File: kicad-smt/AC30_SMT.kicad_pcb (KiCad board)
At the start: 2 copper layers, 173 x 88.5 mm, 122 parts, among them IC1 4013, IC10 555, IC11 4001, IC12 1489, IC13 4070, IC14 4053, IC15 1488, IC2 4001, IC3 4070, IC4 4558, IC5 4013, IC6 4053, IC7 4049, IC8 4013, IC9 4023, J1 SWITCHES, J12 Power input, J13 MOTOR, J14 MIC, J15 EAR, J2 LEDS, J3 Computer interface (COMP), J4 Control interface, J5 Terminal interface (TERM), Q1 MMBT5088, Q10 MMBT5087, Q11 MMBT5087, Q2 MMBT5088, Q3 MMBT5087, Q4 MMBT5088, Q5 MMBT5088, Q6 MMBT5088, Q7 MMBT5088, Q8 MMBT5088, Q9 MMBT5087

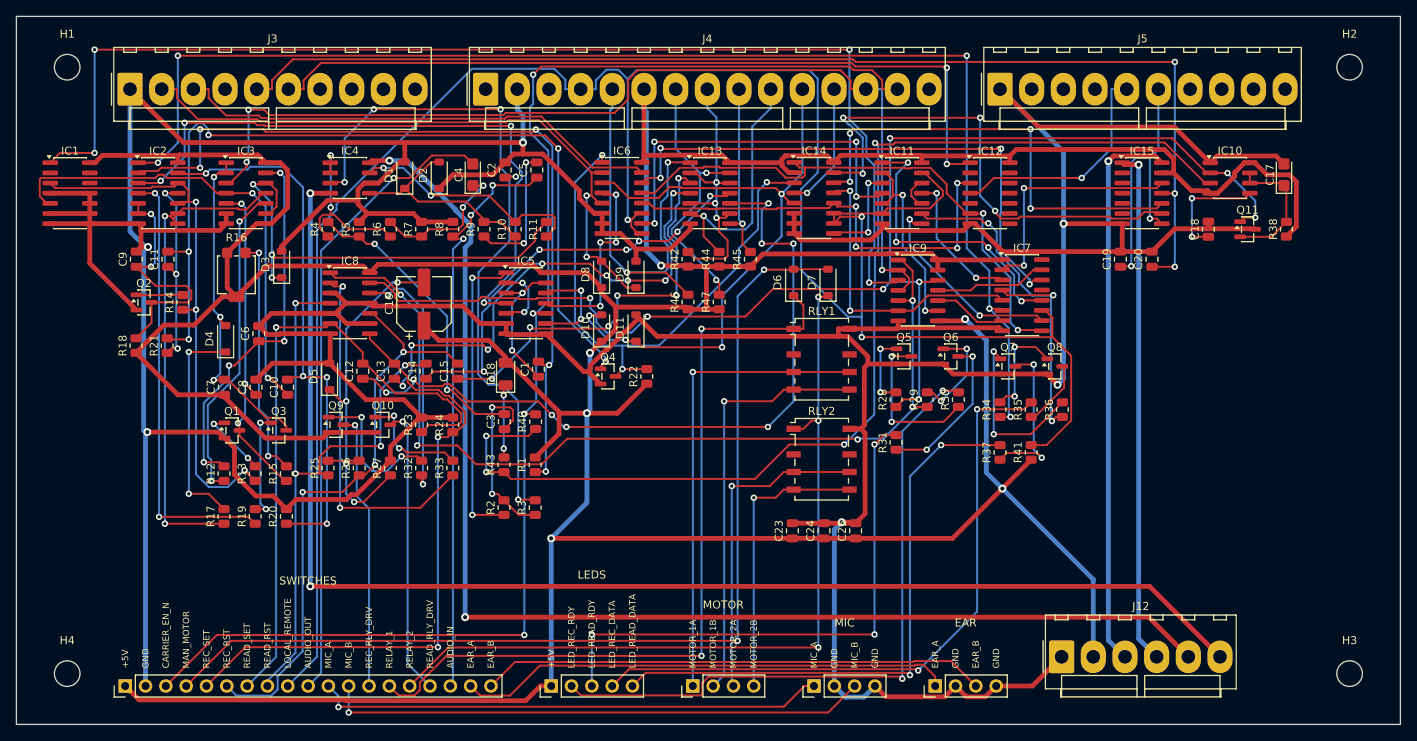
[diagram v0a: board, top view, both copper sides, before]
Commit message: Add a GND copper fill to both boards
tools/zones.py adds a GND zone on F.Cu and B.Cu over the whole outline
(0.3 mm clearance, 0.25 mm min width, 0.5/0.5 mm thermal reliefs, islands
removed); build.sh fills it with kicad-cli after routing. GND pads whose
thermal relief is starved get a solid connection, refilling until none is
left (11 pads through-hole, 2 SMT). FILL=0 builds without it.
Both boards ERC/DRC (all severities)/parity clean; Gerbers regenerated;
settings docs and README updated.

Co-Authored-By: Claude Opus 5.5 <noreply@anthropic.com>
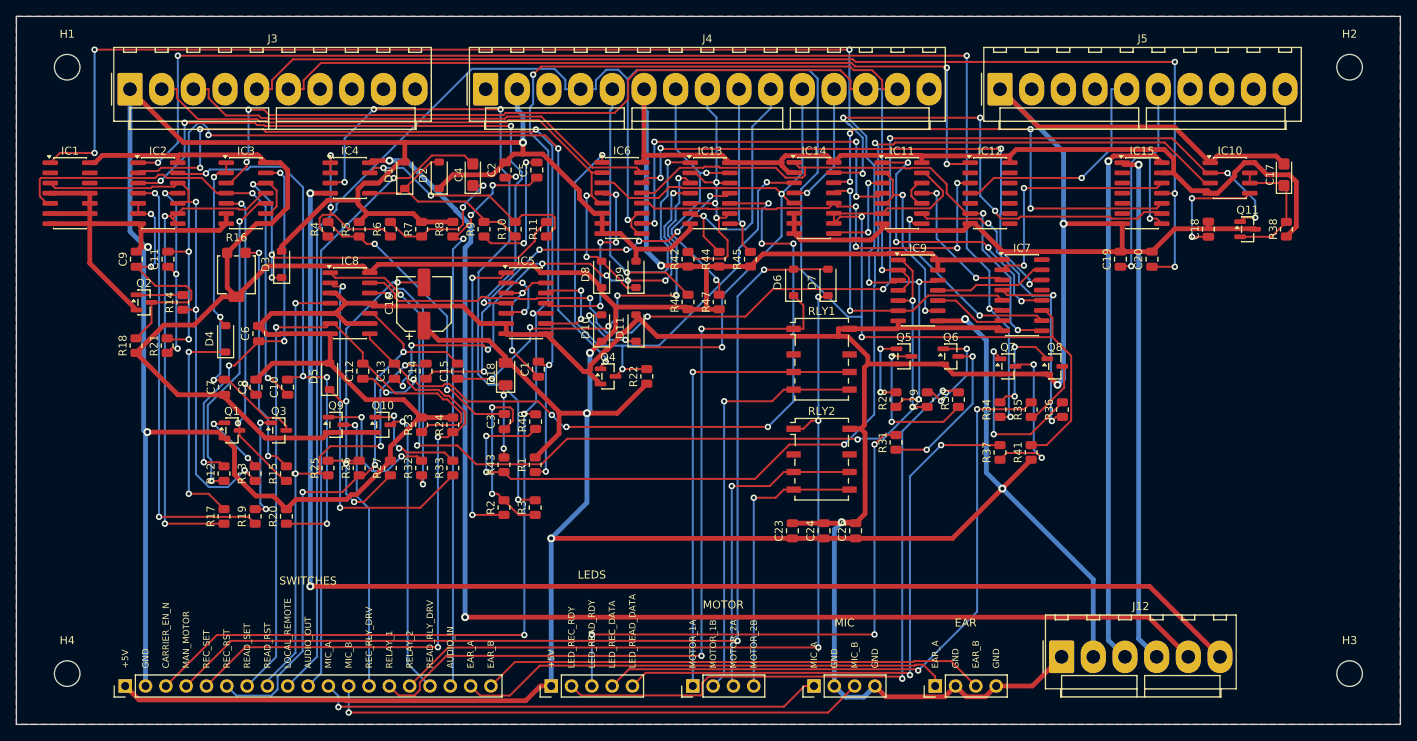
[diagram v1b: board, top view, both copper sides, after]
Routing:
- added copper zone on B.Cu, net GND
- added copper zone on F.Cu, net GND

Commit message: Motor and relay nets in the Power netclass
MOTOR_1A/1B/2A/2B and RELAY_1/2 now route as 0.6 mm tracks with 1.0/0.5 mm
vias (POWER_CLASS in pcb.py; placement unchanged). Both boards rebuilt:
routed on the first attempt, GND fill, ERC/DRC (all severities)/parity
clean. Gerbers regenerated; settings docs updated.

Co-Authored-By: Claude Opus 5.5 <noreply@anthropic.com>
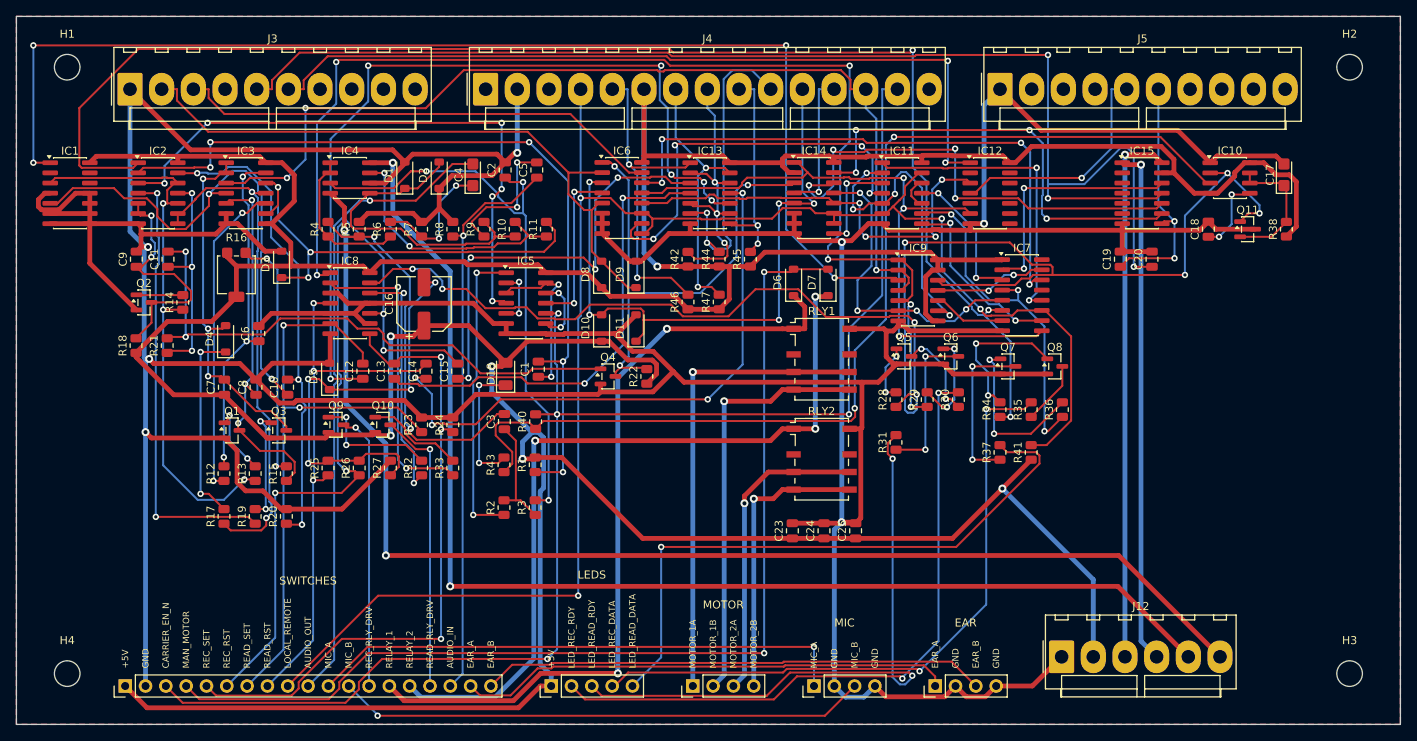
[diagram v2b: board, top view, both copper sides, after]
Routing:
- net /LOCAL_REMOTE: track 276.2 -> 205.9 mm, vias 3 -> 4
- net /Mod/Demod & power input/DEM_Q4B: track 109.9 -> 71.5 mm, vias 5 -> 2
- net GND: track 749.6 -> 785.4 mm, vias 6 -> 7
- net /READ_EN: track 119.1 -> 151.4 mm, vias 5 -> 6
- net /REC_RST: track 73.3 -> 102.4 mm, vias 3 -> 4
- net /REC_EN: track 167.4 -> 192.7 mm
- net /STOP_READ_P: track 52.9 -> 73.3 mm, vias 6 -> 4
- net /CPU_RS232_IN: track 147.2 -> 163.4 mm
- net /READ_ACTIVE_N: track 23.9 -> 38.8 mm, vias 2 -> 4
- net /Mod/Demod & power input/MOD_F2: track 86.6 -> 72.9 mm, vias 5 -> 3
- net /STOP_RECORD: track 54.8 -> 41.3 mm
- net /Mod/Demod & power input/DEM_IN: track 26.8 -> 40.2 mm
- net /TERM_DATA: track 69.9 -> 83.3 mm, vias 2 -> 3
- net /READ_RST: track 82.2 -> 68.9 mm, vias 4 -> 3
- net /START_READ_P: track 93.4 -> 105.6 mm, vias 8 -> 6
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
